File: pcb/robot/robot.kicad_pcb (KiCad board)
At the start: 4 copper layers, 80 x 70 mm, 406 parts, among them IC1 TPS22998RYZR, J1 USB4151-GF-C, J3 USBC_Receptacle_SMD_RA, J4 Conn_01x02, J6 Conn_01x06_MountingPin, J7 Conn_01x06_MountingPin, J9 Conn_01x05, Q1 Q_NMOS_GDS, Q2 AS2312, Q3 YJL3416A, Q4 Q_NMOS_GDS, Q5 EFC8811R-TF, Q6 SN74AHC125RGYR, Q7 AO3400A, SW1 SW_SPST, U1 AP2502KTR-G1, U10 TPD1E05U06, U11 MAX77958EWV+T, U12 TPS22950CDDCR, U13 TPS61253AYFFT, U14 NCP3901, U15 TPD1E05U06, U16 TVS0500DRV, U17 TPD1E05U06, U18 TPD1E05U06, U19 TPD1E05U06, U2 TPS63021DSJR, U20 AP33771DKZ-13, U21 LSF0102DCTR, U22 BQ27742YZFR-G1, U23 MAX77857BEWB+, U24 W25Q128JVS, U25 DRV8830DRCR, U26 DRV8830DRCR, U27 STWLC38JRM, U28 MAX77976EFD+, U29 RP2040, U3 XC6206PxxxMR, U30 TPS3808G01DBVR, U31 TPS3808G01DBVR, U32 MCP6541T-I/OT, U33 MAX6006AEUR+T, U34 MCP6541T-I/OT, U4 TPD1E05U06, U5 TPD1E05U06, U6 TVS0500DRV, U7 TPD1E05U06, U8 TPD1E05U06, U9 TPD1E05U06, Y1 ECS-120-8-36-CKM-TR3

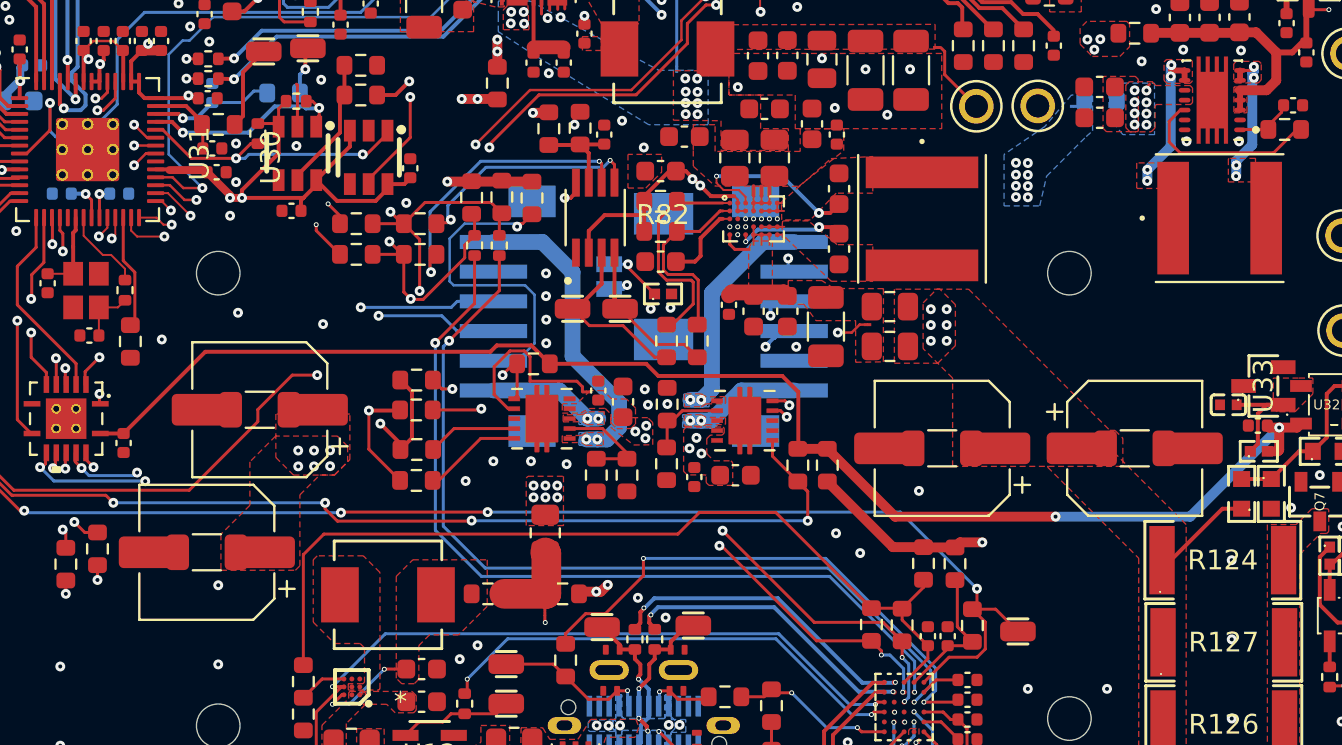
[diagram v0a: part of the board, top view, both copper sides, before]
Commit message: Populate 2 of 4 motor-VCC bulk caps with real 100uF/16V parts (#25)
C132 and C134 (nearest each DRV8830) now use the real
APXK160ARA101MF611 (NCC, 100uF/16V/24mOhm ESR/2.49A ripple) instead
of a mismatched BOM entry that pointed to an unrelated 1206 ceramic
part. C133/C135 stay DNP for bring-up tuning, same part assigned to
keep BOM data consistent across all four positions.

Verified via kicad-cli: ERC +4 (cosmetic lib-symbol-mismatch warnings,
same class as the pre-existing U12 issue), DRC 0 unconnected, same
single pre-existing parity warning, net -7 DRC warnings overall.
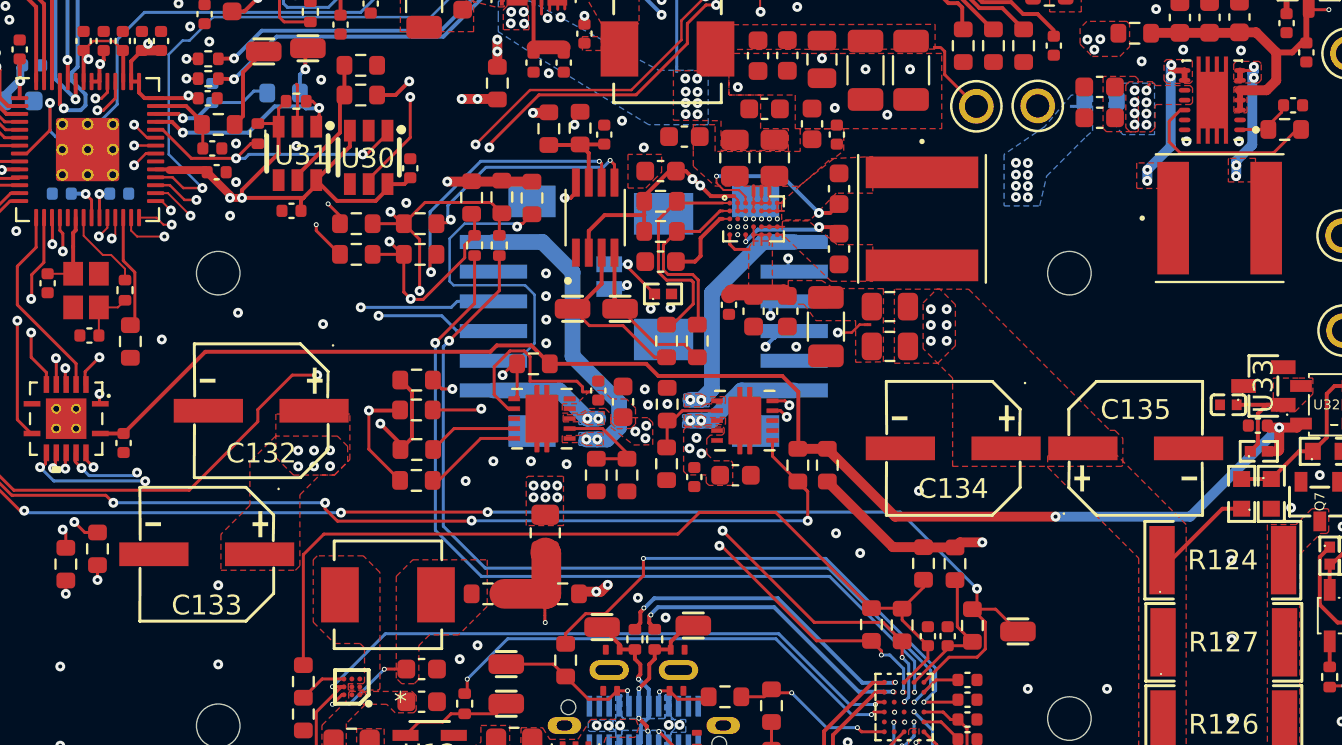
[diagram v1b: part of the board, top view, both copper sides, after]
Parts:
- C132, C133, C134, C135: value 100uF -> APXK160ARA101MF611; footprint robot:CP_Elec_APXJ100ARA271MF61G -> easyeda2kicad:CAP-SMD_BD6.3-L6.6-W6.6-FD
- moved C135 44.3 mm to (124.8, 138.8), turned to 0 degrees
- moved C132 44.2 mm to (80.7, 136.9), turned to 180 degrees
- moved C134 38.1 mm to (115.6, 138.8)
- moved C133 37.5 mm to (77.9, 144.2)

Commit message: Gate MAX77857 EN via GPIO22 divider, bump C136 to 100nF (#24)
R135/R136 (10k/10k) now gate U23.EN from GPIO22 instead of tying it
straight to 1.8V. GPIO22 low or floating (RP2040 reset/boot default)
holds EN at 0V, no firmware dependency for the off-state. VIO stays
on 1.8V, untouched. C136 220pF -> 100nF (CL05A104KA5NNNC) to meet
the MAX6006's real >=10nF minimum.

Verified against baseline: ERC 337/337 (no new violations), DRC 0
unconnected items, no violations tied to the new parts.
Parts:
- added R135: 10k, robot:R_0603_1608Metric, F.Cu at (83.9, 130.6)
- added R136: 10k, robot:R_0603_1608Metric, F.Cu at (83.9, 132.2)
- C136: value 220pF -> 0.1uF; footprint easyeda2kicad:C0402 -> robot:C_0402_1005Metric
- moved C136 0.08 mm to (129.5, 136.7), turned to 0 degrees
- moved R126 0.07 mm to (129.2, 152.8)
- moved R127 0.07 mm to (129.2, 148.7)
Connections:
- C136 pad 1: Net-(U32-VIN-) -> GND
- C136 pad 2: GND -> Net-(U32-VIN-)
- U23 pad B2: /BoostRegulator/1V8 -> Net-(R135-Pad2)
- U23 pad B3: /BoostRegulator/1V8 -> Net-(R135-Pad2)
- U29 pad 34: /MCU/GPIO22 -> /GPIO22
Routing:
- net Net-(R135-Pad2): track 0.00 -> 26.8 mm, vias 0 -> 2
- net /GPIO22: track 0.00 -> 13.5 mm
- net /BoostRegulator/1V8: track 58.6 -> 57.3 mm
- net /MCU/UART_RX: track 39.8 -> 40.5 mm
- net /MCU/UART_TX: track 40.0 -> 39.4 mm
